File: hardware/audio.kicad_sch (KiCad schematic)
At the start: 6 parts, among them U9 MAX98357A

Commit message: Fix gain selector resistor footprint
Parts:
- R36: footprint lib:SKRHABE010_ALPS -> Resistor_SMD:R_0603_1608Metric
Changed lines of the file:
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@@
 	(label "AUDIO.BCLK"
 		(at 127 91.44 0)
+		(fields_autoplaced yes)
 		(effects
 			(font
@@
 	(label "AUDIO.SD"
 		(at 127 88.9 0)
+		(fields_autoplaced yes)
 		(effects
 			(font
@@
 	(label "AUDIO.LRCLK"
 		(at 127 93.98 0)
+		(fields_autoplaced yes)
 		(effects
 			(font
@@
 			)
 		)
-		(property "Footprint" "lib:SKRHABE010_ALPS"
+		(property "Footprint" "Resistor_SMD:R_0603_1608Metric"
 			(at 124.46 113.538 90)
 			(effects

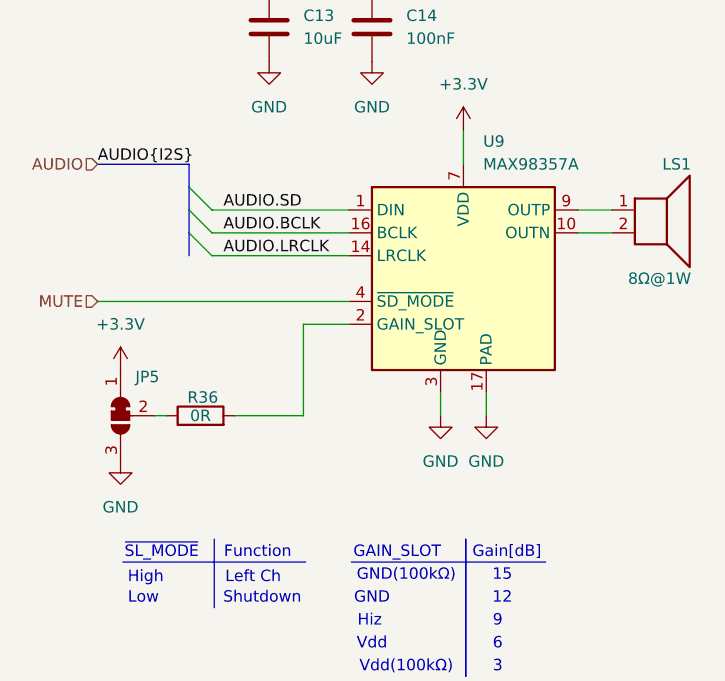
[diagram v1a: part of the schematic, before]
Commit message: Route the audio subsystem
Fix BMS routing
Remove audio gain selection, to relax routing
Add DRC rule for JLC
Add custom rule for Audio BGA routing
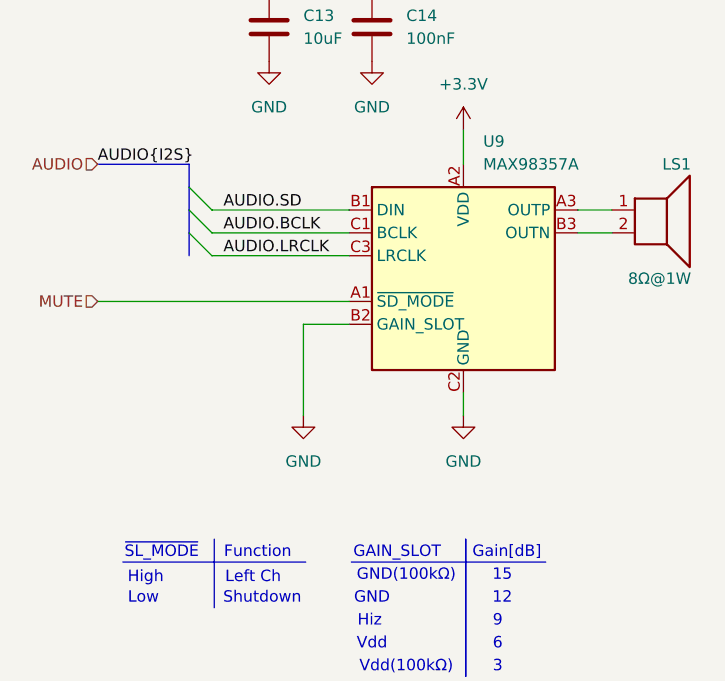
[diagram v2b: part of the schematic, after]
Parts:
- removed JP5: EN1, Jumper:SolderJumper-3_P1.3mm_Bridged12_RoundedPad1.0x1.5mm, symbol Jumper:SolderJumper_3_Bridged12
- removed R36: 0R, Resistor_SMD:R_0603_1608Metric, symbol Device:R
- U9: footprint Package_DFN_QFN:TQFN-16-1EP_3x3mm_P0.5mm_EP1.23x1.23mm -> Package_BGA:WLP-9_1.448x1.468mm_Layout3x3_P0.4mm_Ball0.27mm_Pad0.25mm
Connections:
- net +3.3V: now also U9.A2 (VDD); no longer U9.7 (VDD), U9.8 (VDD)
- net AUDIO.BCLK: now also U9.C1 (BCLK); no longer U9.16 (BCLK)
- net AUDIO.LRCLK: now also U9.C3 (LRCLK); no longer U9.14 (LRCLK)
- net AUDIO.SD: now also U9.B1 (DIN); no longer U9.1 (DIN)
- net GND: now also U9.B2 (GAIN_SLOT), U9.C2 (GND); no longer U9.11 (GND), U9.15 (GND), U9.17 (PAD), U9.3 (GND)
- net MUTE: now also U9.A1 (~{SD_MODE}); no longer U9.4 (~{SD_MODE})
- net at LS1.2: now also U9.B3 (OUTN); no longer U9.10 (OUTN)
- net at LS1.1: now also U9.A3 (OUTP); no longer U9.9 (OUTP)

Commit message: Cleanup project library
Add hexpansion connector symbol, footprint and 3d
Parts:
- LS1: footprint lib:KLJ-01304T-08R07W -> badge:KLJ-01304T-08R07W
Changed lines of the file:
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@@
 			)
 		)
-		(property "Footprint" "lib:KLJ-01304T-08R07W"
+		(property "Footprint" "badge:KLJ-01304T-08R07W"
 			(at 175.26 93.98 0)
 			(effects

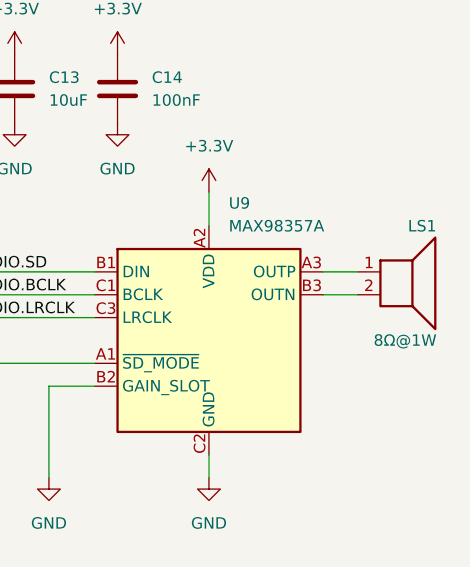
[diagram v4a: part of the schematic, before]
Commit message: Add sdcard fooprint
Remove io expander
Reorganize a bit the mcu schematic
Routed audio
Routed lora
Partial pin swapping of esp32 for facilitating routing
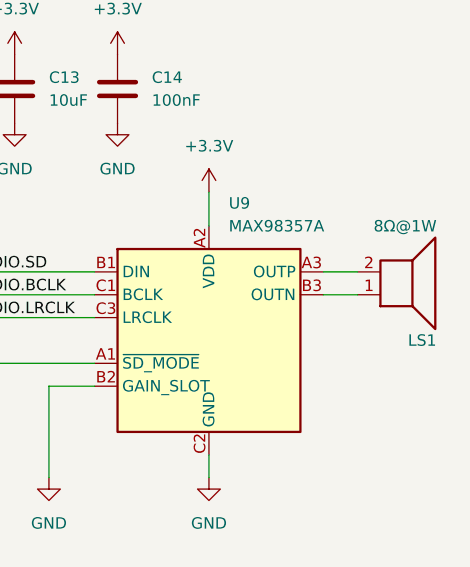
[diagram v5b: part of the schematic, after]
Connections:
- net at U9.A3 (OUTP): now also LS1.2; no longer LS1.1
- net at U9.B3 (OUTN): now also LS1.1; no longer LS1.2
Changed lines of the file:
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@@
+		)
+	)
+	(bus
+		(pts
+			(xy 123.19 91.44) (xy 123.19 93.98)
+		)
+		(stroke
+			(width 0)
+			(type default)
 		)
 	)
 	(wire
 		(pts
+			(xy 135.89 101.6) (xy 140.97 101.6)
+		)
+		(stroke
+			(width 0)
+			(type default)
+		)
+	)
+	(polyline
+		(pts
+			(xy 153.924 125.476) (xy 153.924 140.716)
+		)
+		(stroke
+			(width 0)
+			(type default)
+		)
+	)
+	(bus
+		(pts
+			(xy 113.03 83.82) (xy 123.19 83.82)
+		)
+		(stroke
+			(width 0)
+			(type default)
+		)
+	)
+	(wire
+		(pts
+			(xy 125.73 91.44) (xy 140.97 91.44)
+		)
+		(stroke
+			(width 0)
+			(type default)
+		)
+	)
+	(polyline
+		(pts
+			(xy 153.924 125.476) (xy 153.924 125.476)
+		)
+		(stroke
+			(width 0)
+			(type default)
+		)
+	)
+	(polyline
+		(pts
+			(xy 141.224 128.016) (xy 162.814 128.016)
+		)
+		(stroke
+			(width 0)
+			(type default)
+		)
+	)
+	(wire
+		(pts
+			(xy 125.73 88.9) (xy 140.97 88.9)
+		)
+		(stroke
+			(width 0)
+			(type default)
+		)
+	)
+	(bus
+		(pts
+			(xy 123.19 86.36) (xy 123.19 88.9)
+		)
+		(stroke
+			(width 0)
+			(type default)
+		)
+	)
+	(wire
+		(pts
 			(xy 170.18 88.9) (xy 166.37 88.9)
-		)
-		(stroke
-			(width 0)
-			(type default)
-		)
-	)
-	(bus
-		(pts
-			(xy 123.19 91.44) (xy 123.19 93.98)
-		)
-		(stroke
-			(width 0)
-			(type default)
-		)
-	)
-	(wire
-		(pts
-			(xy 135.89 101.6) (xy 140.97 101.6)
-		)
-		(stroke
-			(width 0)
-			(type default)
-		)
-	)
-	(polyline
-		(pts
-			(xy 153.924 125.476) (xy 153.924 140.716)
-		)
-		(stroke
-			(width 0)
-			(type default)
-		)
-	)
-	(bus
-		(pts
-			(xy 113.03 83.82) (xy 123.19 83.82)
-		)
-		(stroke
-			(width 0)
-			(type default)
-		)
-	)
-	(wire
-		(pts
-			(xy 125.73 91.44) (xy 140.97 91.44)
-		)
-		(stroke
-			(width 0)
-			(type default)
-		)
-	)
-	(polyline
-		(pts
-			(xy 153.924 125.476) (xy 153.924 125.476)
-		)
-		(stroke
-			(width 0)
-			(type default)
-		)
-	)
-	(polyline
-		(pts
-			(xy 141.224 128.016) (xy 162.814 128.016)
-		)
-		(stroke
-			(width 0)
-			(type default)
-		)
-	)
-	(wire
-		(pts
-			(xy 125.73 88.9) (xy 140.97 88.9)
-		)
-		(stroke
-			(width 0)
-			(type default)
-		)
-	)
-	(bus
-		(pts
-			(xy 123.19 86.36) (xy 123.19 88.9)
 		)
 		(stroke
@@
 	(symbol
 		(lib_id "Device:Speaker")
-		(at 175.26 88.9 0)
+		(at 175.26 91.44 0)
+		(mirror x)
 		(unit 1)
 		(exclude_from_sim no)
@@
 		(dnp no)
 		(property "Reference" "LS1"
-			(at 175.768 83.82 0)
+			(at 175.768 96.52 0)
 			(effects
 				(font
@@
 		)
 		(property "Value" "8Ω@1W"
-			(at 171.958 96.52 0)
+			(at 171.958 83.82 0)
 			(effects
 				(font
@@
 		)
 		(property "Footprint" "badge:KLJ-01304T-08R07W"
-			(at 175.26 93.98 0)
+			(at 175.26 86.36 0)
 			(effects
 				(font
@@
 		)
 		(property "Description" "Speaker"
-			(at 175.26 88.9 0)
+			(at 175.26 91.44 0)
 			(effects
 				(font
@@
 		)
 		(property "LCSC" "C18186315"
-			(at 175.26 88.9 0)
-			(effects
-				(font
+			(at 175.26 91.44 0)
+			(effects
+				(font

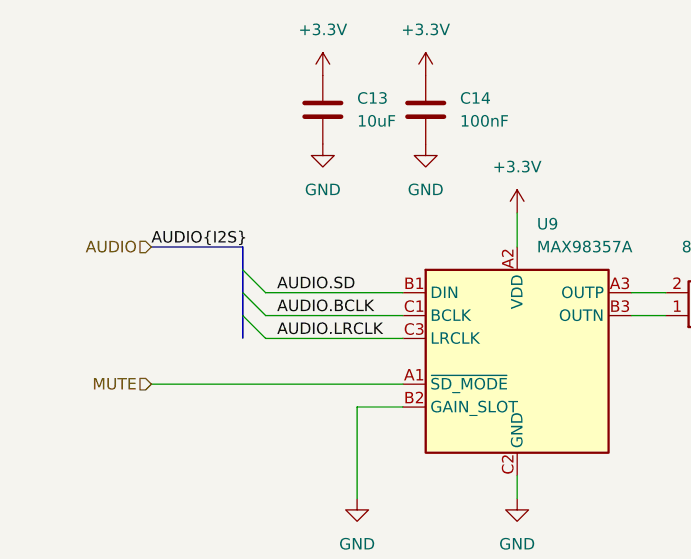
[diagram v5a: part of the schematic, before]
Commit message: Route all board
Fix CS missing for SD card
Add IMU symbol and footprint to the project lib
Finish esp32 pinswaps
Move non critical signals to the keyboard IO expander
Add power flag symbols
Fix Dpad pin type
Fix IMU pin type
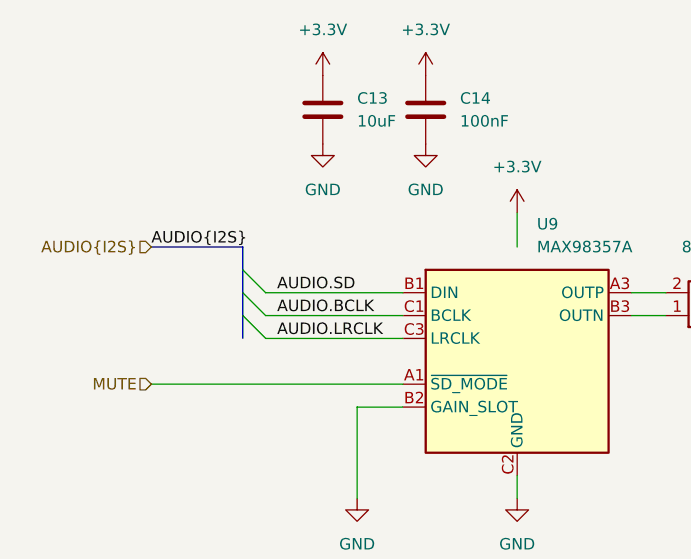
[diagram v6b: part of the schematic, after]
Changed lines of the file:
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@@
 		)
 	)
-	(hierarchical_label "AUDIO"
+	(hierarchical_label "AUDIO{I2S}"
 		(shape input)
 		(at 113.03 83.82 180)
@@
 			)
 		)
+		(pin "B2"
+		)
+		(pin "C2"
+		)
+		(pin "B1"
+		)
+		(pin "B3"
+		)
+		(pin "C1"
+		)
+		(pin "A2"
+		)
 		(pin "A3"
 		)
-		(pin "B2"
-		)
 		(pin "C3"
 		)
-		(pin "C1"
-		)
-		(pin "B3"
-		)
 		(pin "A1"
 		)
-		(pin "B1"
-		)
-		(pin "C2"
-		)
-		(pin "A2"
-		)
-		(instances
+		(instances

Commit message: Associate all LCSC component
Change sdcard pullup resistor to 47K
Center main schematic
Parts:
- C13: LCSC (none) -> C1691
- U9: LCSC (none) -> C2682619
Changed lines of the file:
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@@
+			)
+		)
+		(property "LCSC" "C1691"
+			(at 132.08 68.58 0)
+			(effects
+				(font
+					(size 1.27 1.27)
+				)
+				(hide yes)
 			)
 		)
@@
 			(at 153.67 96.52 0)
 			(effects
+				(font
+					(size 1.27 1.27)
+				)
+				(hide yes)
+			)
+		)
+		(property "LCSC" "C2682619"
+			(at 153.67 96.52 0)
+			(effects

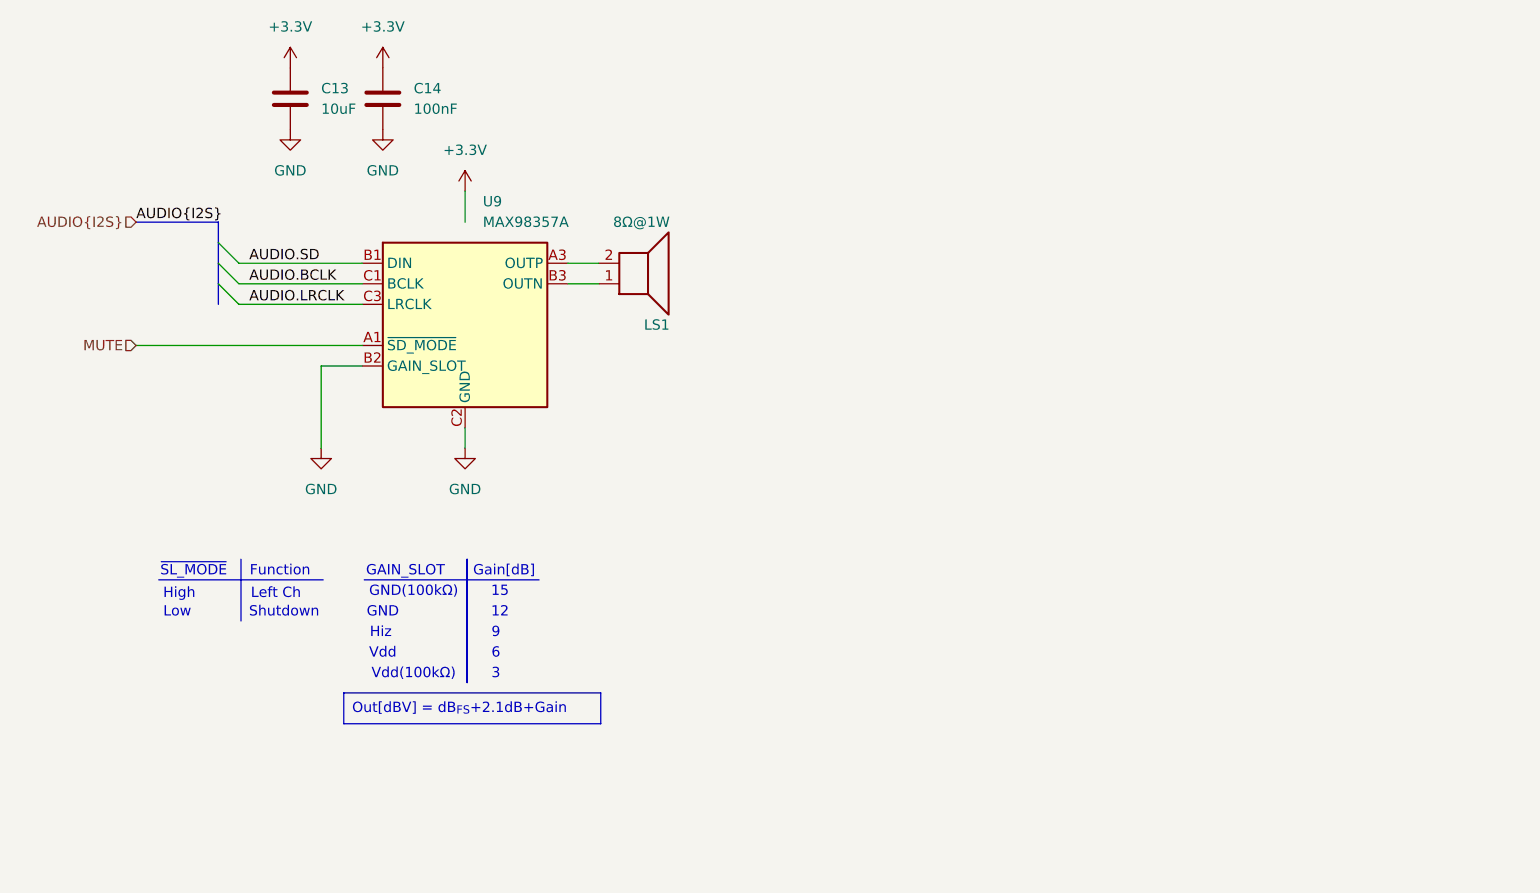
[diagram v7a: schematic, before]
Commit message: Beautified schematic, added I2C addresses
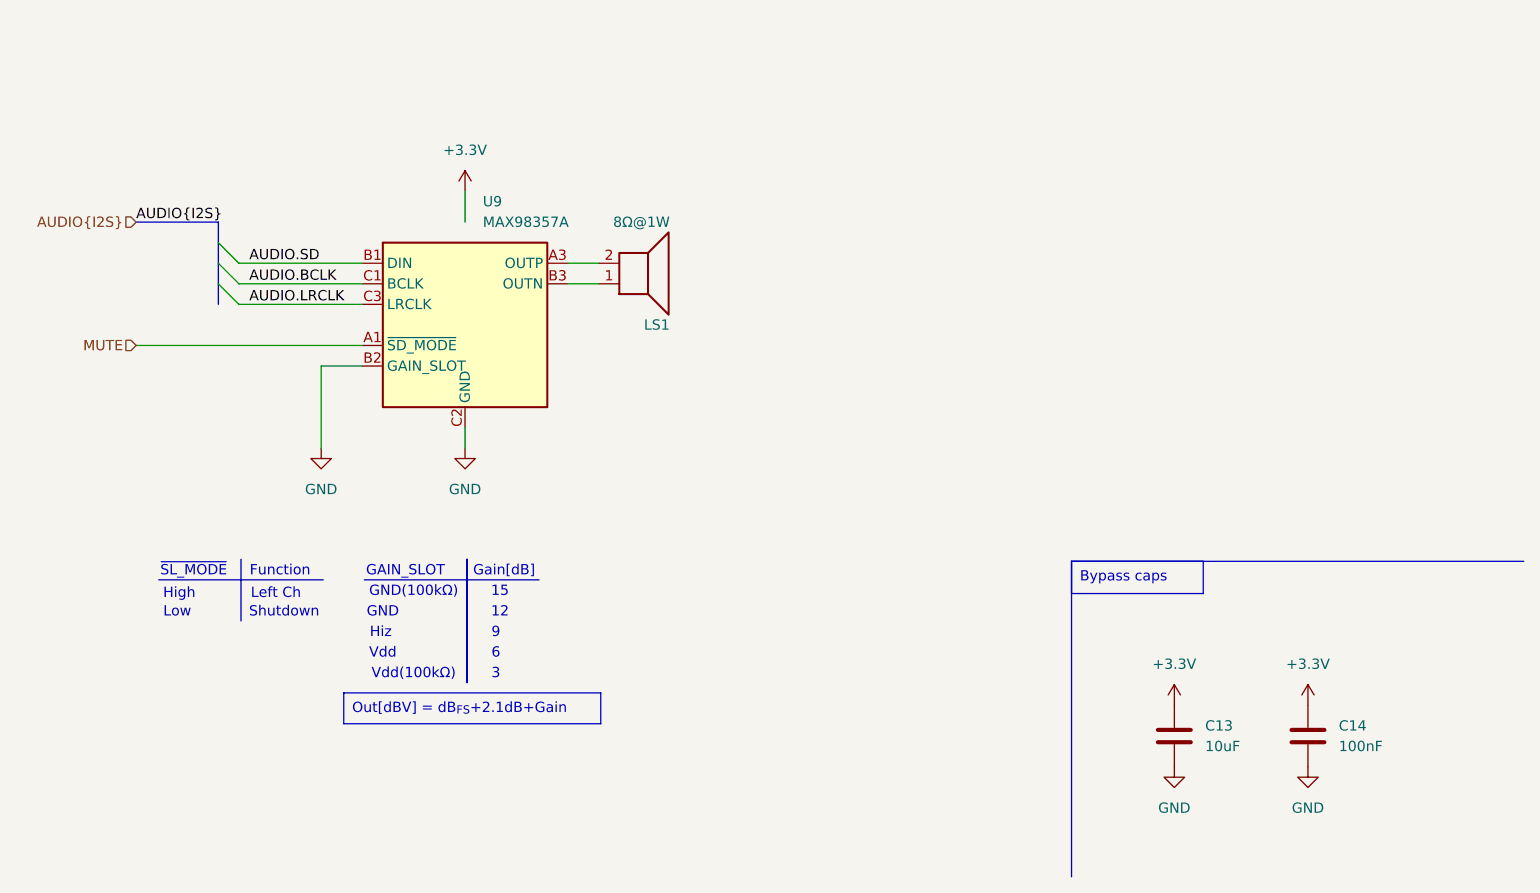
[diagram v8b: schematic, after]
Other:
- moved on the sheet: C13, C14
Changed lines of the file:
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@@
+		)
+	)
+	(polyline
+		(pts
+			(xy 228.6 125.73) (xy 284.48 125.73)
+		)
+		(stroke
+			(width 0)
+			(type default)
 		)
 	)
@@
 		(pts
 			(xy 141.224 128.016) (xy 162.814 128.016)
+		)
+		(stroke
+			(width 0)
+			(type default)
+		)
+	)
+	(polyline
+		(pts
+			(xy 228.6 164.7089) (xy 228.6 125.73)
 		)
 		(stroke
@@
 		(at 138.684 141.986 0)
 		(size 31.75 3.81)
+		(stroke
+			(width 0)
+			(type default)
+		)
+		(fill
+			(type none)
+		)
+		(effects
+			(font
+				(size 1.27 1.27)
+			)
+			(justify left top)
+		)
+	)
+	(text_box "Bypass caps"
+		(exclude_from_sim no)
+		(at 228.6 125.73 0)
+		(size 16.2714 3.98)
 		(stroke
 			(width 0)
@@
 	(symbol
 		(lib_id "Device:C")
-		(at 143.51 68.58 0)
+		(at 257.81 147.32 0)
 		(unit 1)
 		(exclude_from_sim no)
@@
 		(fields_autoplaced yes)
 		(property "Reference" "C14"
-			(at 147.32 67.3099 0)
+			(at 261.62 146.0499 0)
 			(effects
 				(font
@@
 		)
 		(property "Value" "100nF"
-			(at 147.32 69.8499 0)
+			(at 261.62 148.5899 0)
 			(effects
 				(font
@@
 		)
 		(property "Footprint" "Capacitor_SMD:C_0402_1005Metric"
-			(at 144.4752 72.39 0)
+			(at 258.7752 151.13 0)
 			(effects
 				(font
@@
 		)
 		(property "Datasheet" "~"
-			(at 143.51 68.58 0)
+			(at 257.81 147.32 0)
 			(effects
 				(font
@@
 		)
 		(property "Description" "Unpolarized capacitor"
-			(at 143.51 68.58 0)
+			(at 257.81 147.32 0)
 			(effects
 				(font
@@
 		)
 		(property "LCSC" "C1525"
-			(at 143.51 68.58 0)
+			(at 257.81 147.32 0)
 			(effects
 				(font
@@
 	(symbol
 		(lib_id "power:+3.3V")
-		(at 132.08 64.77 0)
+		(at 241.3 143.51 0)
 		(unit 1)
 		(exclude_from_sim no)
@@
 		(fields_autoplaced yes)
 		(property "Reference" "#PWR090"
-			(at 132.08 68.58 0)
+			(at 241.3 147.32 0)
 			(effects
 				(font
@@
 		)
 		(property "Value" "+3.3V"
-			(at 132.08 59.69 0)
+			(at 241.3 138.43 0)
 			(effects
 				(font
@@
 		)
 		(property "Footprint" ""
-			(at 132.08 64.77 0)
+			(at 241.3 143.51 0)
 			(effects
 				(font
@@
 		)
 		(property "Datasheet" ""
-			(at 132.08 64.77 0)
+			(at 241.3 143.51 0)
 			(effects
 				(font
@@
 		)
 		(property "Description" "Power symbol creates a global label with name \"+3.3V\""
-			(at 132.08 64.77 0)
+			(at 241.3 143.51 0)
 			(effects
 				(font
@@
 	(symbol
 		(lib_id "power:GND")
-		(at 143.51 72.39 0)
+		(at 257.81 151.13 0)
 		(unit 1)
 		(exclude_from_sim no)
@@
 		(fields_autoplaced yes)
 		(property "Reference" "#PWR093"
-			(at 143.51 78.74 0)
+			(at 257.81 157.48 0)
 			(effects
 				(font
@@
 		)
 		(property "Value" "GND"
-			(at 143.51 77.47 0)
+			(at 257.81 156.21 0)
 			(effects
 				(font
@@
 		)
 		(property "Footprint" ""
-			(at 143.51 72.39 0)
+			(at 257.81 151.13 0)
 			(effects
 				(font
@@
 		)
 		(property "Datasheet" ""
-			(at 143.51 72.39 0)
+			(at 257.81 151.13 0)
 			(effects
 				(font
@@
 		)
 		(property "Description" "Power symbol creates a global label with name \"GND\" , ground"
-			(at 143.51 72.39 0)
+			(at 257.81 151.13 0)
 			(effects
 				(font
@@
 	(symbol
 		(lib_id "Device:C")
-		(at 132.08 68.58 0)
+		(at 241.3 147.32 0)
 		(unit 1)
 		(exclude_from_sim no)
@@
 		(fields_autoplaced yes)
 		(property "Reference" "C13"
-			(at 135.89 67.3099 0)
+			(at 245.11 146.0499 0)
 			(effects
 				(font
@@
 		)
 		(property "Value" "10uF"
-			(at 135.89 69.8499 0)
+			(at 245.11 148.5899 0)
 			(effects
 				(font
@@
 		)
 		(property "Footprint" "Capacitor_SMD:C_0603_1608Metric"
-			(at 133.0452 72.39 0)
+			(at 242.2652 151.13 0)
 			(effects
 				(font
@@
 		)
 		(property "Datasheet" "~"
-			(at 132.08 68.58 0)
+			(at 241.3 147.32 0)
 			(effects
 				(font
@@
 		)
 		(property "Description" "Unpolarized capacitor"
-			(at 132.08 68.58 0)
+			(at 241.3 147.32 0)
 			(effects
 				(font
@@
 		)
 		(property "LCSC" "C1691"
-			(at 132.08 68.58 0)
+			(at 241.3 147.32 0)
 			(effects
 				(font
@@
 	(symbol
 		(lib_id "power:+3.3V")
-		(at 143.51 64.77 0)
+		(at 257.81 143.51 0)
 		(unit 1)
 		(exclude_from_sim no)
@@
 		(fields_autoplaced yes)
 		(property "Reference" "#PWR092"
-			(at 143.51 68.58 0)
+			(at 257.81 147.32 0)
 			(effects
 				(font
@@
 		)
 		(property "Value" "+3.3V"
-			(at 143.51 59.69 0)
+			(at 257.81 138.43 0)
 			(effects
 				(font
@@
 		)
 		(property "Footprint" ""
-			(at 143.51 64.77 0)
+			(at 257.81 143.51 0)
 			(effects
 				(font
@@
 		)
 		(property "Datasheet" ""
-			(at 143.51 64.77 0)
+			(at 257.81 143.51 0)
 			(effects
 				(font
@@
 		)
 		(property "Description" "Power symbol creates a global label with name \"+3.3V\""
-			(at 143.51 64.77 0)
+			(at 257.81 143.51 0)
 			(effects
 				(font
@@
 	(symbol
 		(lib_id "power:GND")
-		(at 132.08 72.39 0)
+		(at 241.3 151.13 0)
 		(unit 1)
 		(exclude_from_sim no)
@@
 		(fields_autoplaced yes)
 		(property "Reference" "#PWR091"
-			(at 132.08 78.74 0)
+			(at 241.3 157.48 0)
 			(effects
 				(font
@@
 		)
 		(property "Value" "GND"
-			(at 132.08 77.47 0)
+			(at 241.3 156.21 0)
 			(effects
 				(font
@@
 		)
 		(property "Footprint" ""
-			(at 132.08 72.39 0)
+			(at 241.3 151.13 0)
 			(effects
 				(font
@@
 		)
 		(property "Datasheet" ""
-			(at 132.08 72.39 0)
+			(at 241.3 151.13 0)
 			(effects
 				(font
@@
 		)
 		(property "Description" "Power symbol creates a global label with name \"GND\" , ground"
-			(at 132.08 72.39 0)
-			(effects
-				(font
+			(at 241.3 151.13 0)
+			(effects
+				(font
